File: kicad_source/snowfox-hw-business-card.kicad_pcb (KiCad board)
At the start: 2 copper layers, 85 x 54 mm, 109 parts, among them CN1 Micro_SDCard, CN2 CONN_02X05, CN3 CONN_01X24, CN4 USB_OTG, CN5 CONN_01X14, CN6 CONN_01X04, Q1 SI1304BDL, Q2 BC847, SW1 TAST_VER, SW2 TAST_VER, SW3 TAST_VER, SW4 TAST_VER, SW5 SWITCH_INV, U1 W25Q80D, U2 ATECC608A, U3 FE310-G002, U4 FT230XS, U5 TPS736XX, U6 TPS736XX, U7 M24LR, U8 BMA400, Y1 16MHz

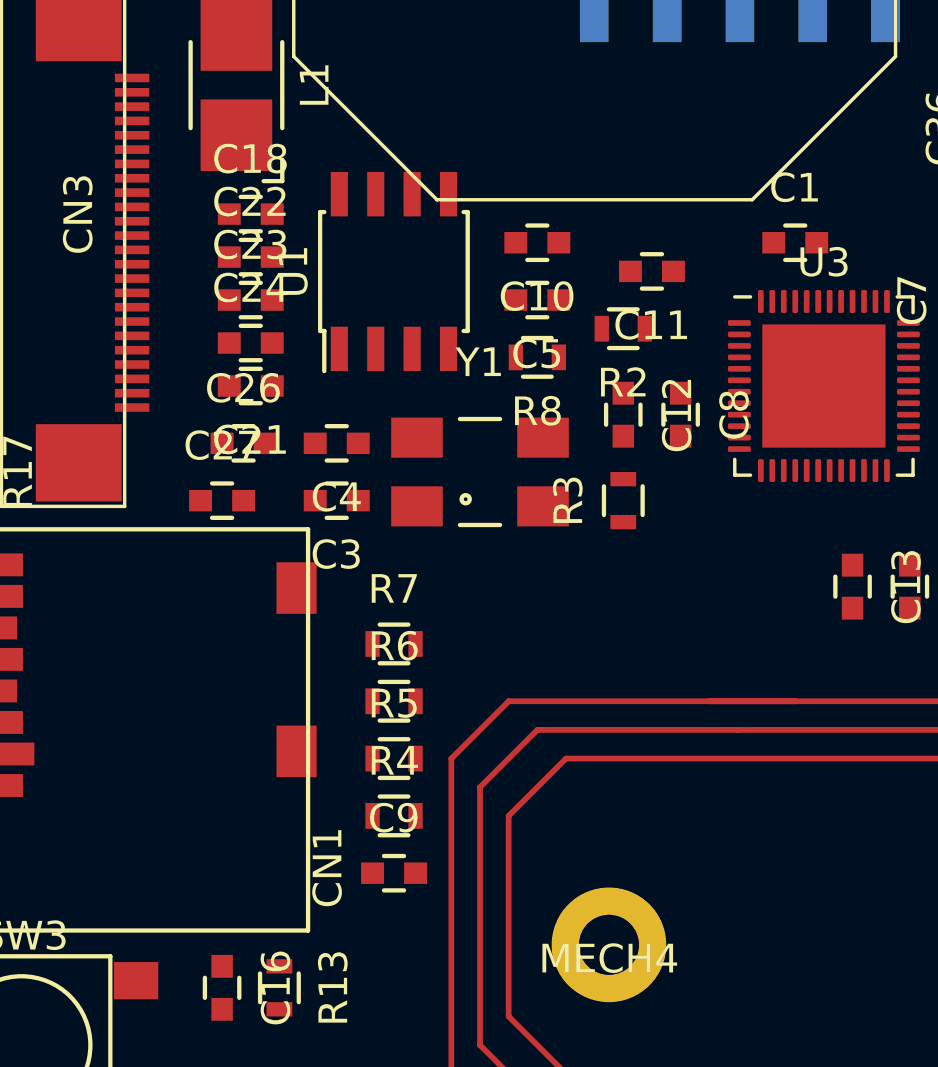
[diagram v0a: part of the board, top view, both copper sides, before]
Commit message: changed to smaller crystal footprint
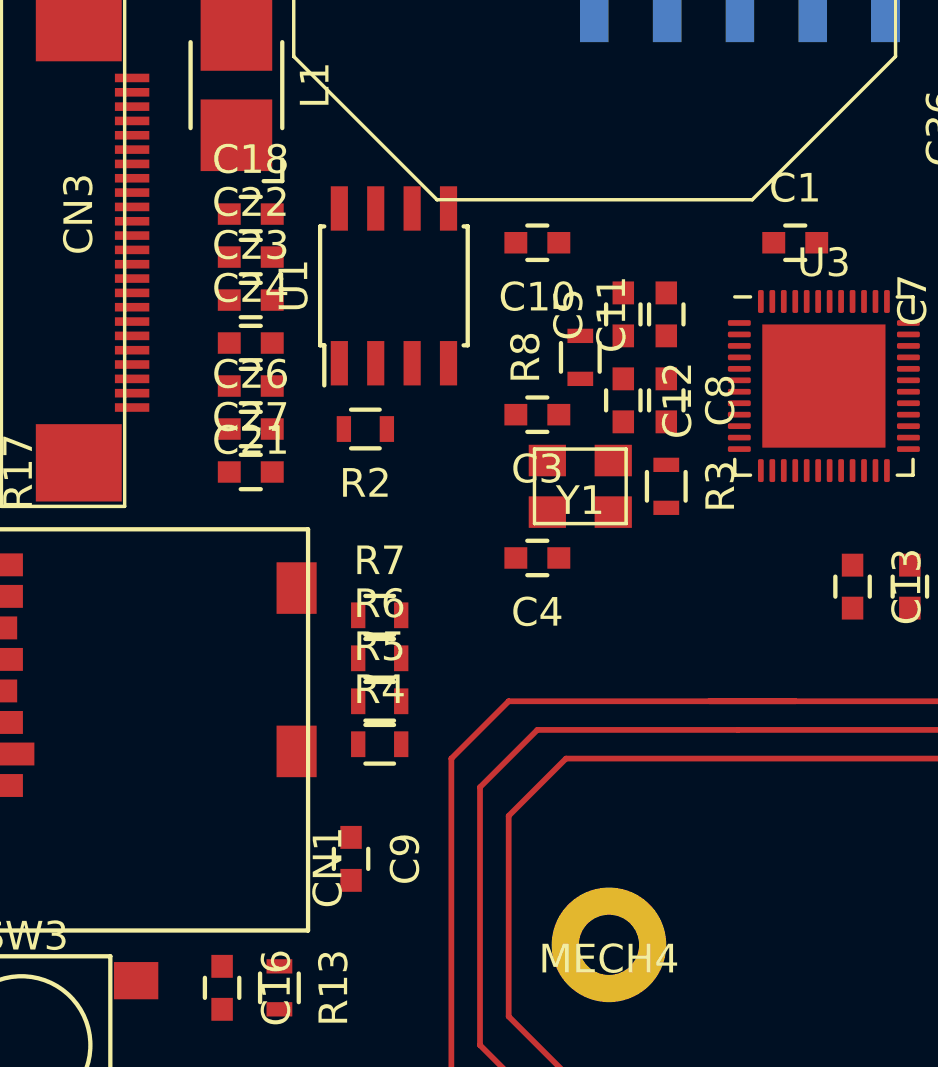
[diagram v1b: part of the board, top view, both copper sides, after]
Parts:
- Y1: footprint crystals:Crystal_SMD_0603_4Pads -> crystals:Crystal_SMD_3.2x2.5mm_4Pad
- moved R2 9.66 mm to (96.0, 111.5)
- moved C4 8.06 mm to (102.0, 116.0)
- moved C3 7.62 mm to (102.0, 111.0)
- moved Y1 3.54 mm to (103.5, 113.5)
- moved C5 3.04 mm to (105.0, 107.5), turned to 90 degrees
- moved R4 2.55 mm to (96.5, 122.5)
- moved R5 2.06 mm to (96.5, 121.0)
- moved C11 1.58 mm to (106.5, 107.5), turned to 90 degrees
- moved C9 1.58 mm to (95.5, 126.5), turned to 270 degrees
- moved R3 1.58 mm to (106.5, 113.5), turned to 270 degrees
- moved R6 1.58 mm to (96.5, 119.5)
- moved R8 1.50 mm to (103.5, 109.0), turned to 90 degrees
- moved C27 1.41 mm to (92.0, 113.0)
- moved R7 1.12 mm to (96.5, 118.0)
- moved C8 0.71 mm to (106.5, 110.5)
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
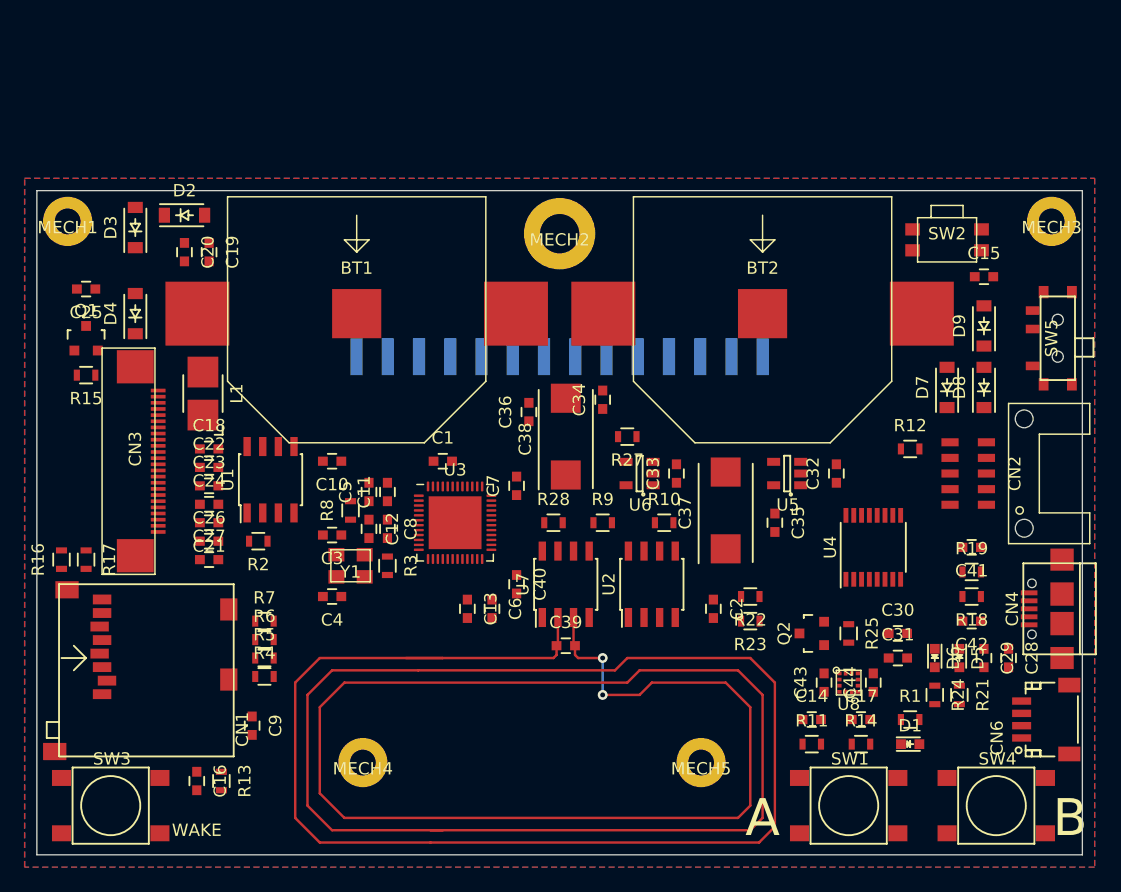
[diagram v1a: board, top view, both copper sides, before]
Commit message: routed some traces
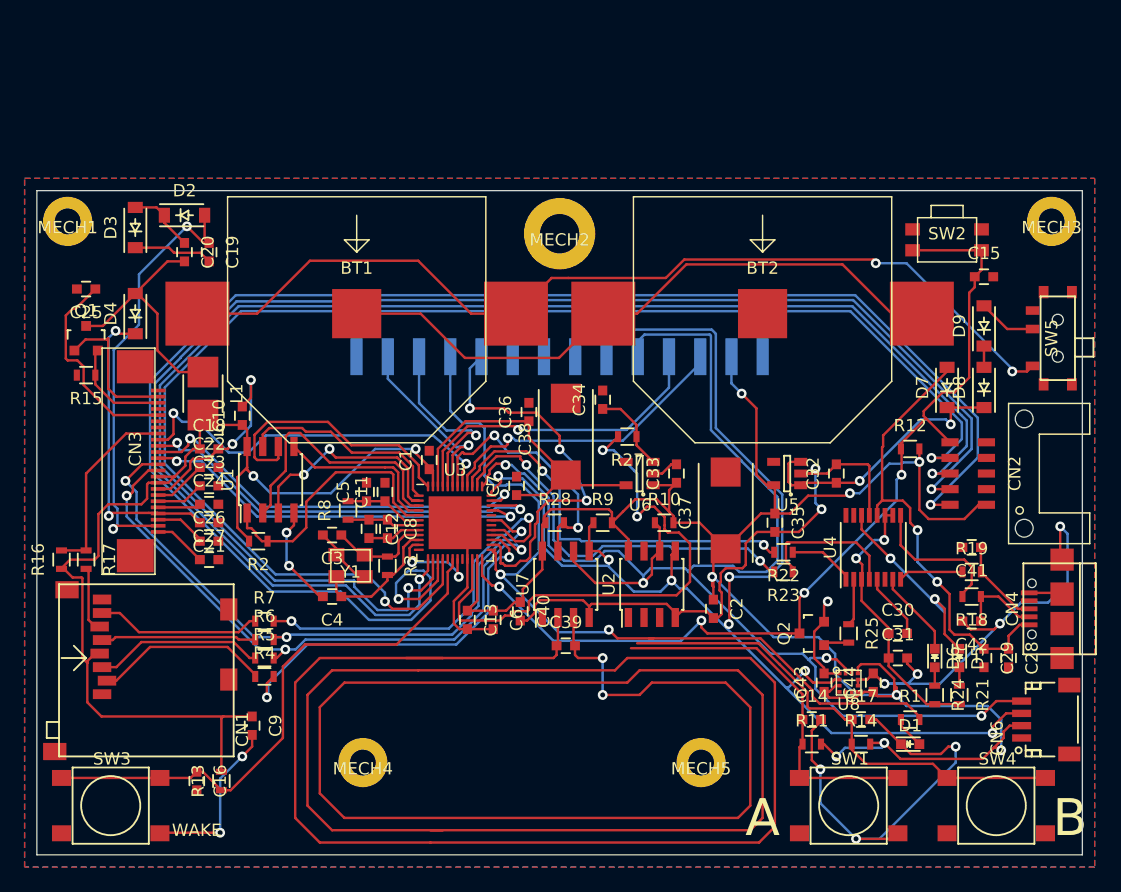
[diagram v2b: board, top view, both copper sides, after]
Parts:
- moved C10 8.18 mm to (94.7, 101.3), turned to 90 degrees
- moved R23 4.83 mm to (138.7, 114.0)
- moved R22 4.50 mm to (138.7, 112.4)
- moved C40 2.22 mm to (117.3, 117.2)
- moved C1 1.10 mm to (109.9, 104.9), turned to 90 degrees
- moved C6 0.91 mm to (115.1, 117.9)
- moved C13 0.90 mm to (113.0, 117.9)
- moved C11 0.20 mm to (106.3, 107.5)
- moved C5 0.20 mm to (104.8, 107.5)
- moved R8 0.20 mm to (103.3, 109.0)
- moved R28 0.10 mm to (120.1, 110.0)
- turned R13 to 90 degrees
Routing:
- net +3V3: track 0.00 -> 256.8 mm, vias 0 -> 12
- net GND: track 0.00 -> 208.4 mm, vias 0 -> 16
- net /Microcontroller/JTAG_TMS: track 0.00 -> 132.6 mm, vias 0 -> 2
- net /Microcontroller/JTAG_TCK: track 0.00 -> 119.5 mm, vias 0 -> 2
- net /Microcontroller/JTAG_TDO: track 0.00 -> 117.1 mm, vias 0 -> 2
- net /Microcontroller/JTAG_TDI: track 0.00 -> 114.0 mm, vias 0 -> 2
- net I2C_SCL: track 0.00 -> 112.4 mm, vias 0 -> 4
- net I2C_SDA: track 0.00 -> 110.5 mm, vias 0 -> 7
- net Net-(BT1-Pad1): track 0.00 -> 77.4 mm, vias 0 -> 2
- net RESET: track 0.00 -> 77.2 mm, vias 0 -> 4
- net /Microcontroller/LED: track 0.00 -> 67.2 mm, vias 0 -> 2
- net /Microcontroller/BUTTON_B: track 0.00 -> 55.1 mm, vias 0 -> 1
- net Net-(BT1-Pad2): track 0.00 -> 52.2 mm
- net SPI_MOSI: track 0.00 -> 51.9 mm, vias 0 -> 3
- net SPI_CLK: track 0.00 -> 51.6 mm, vias 0 -> 3
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
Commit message: changed diodes to smaller footprint, connected all lines in layout, updated images
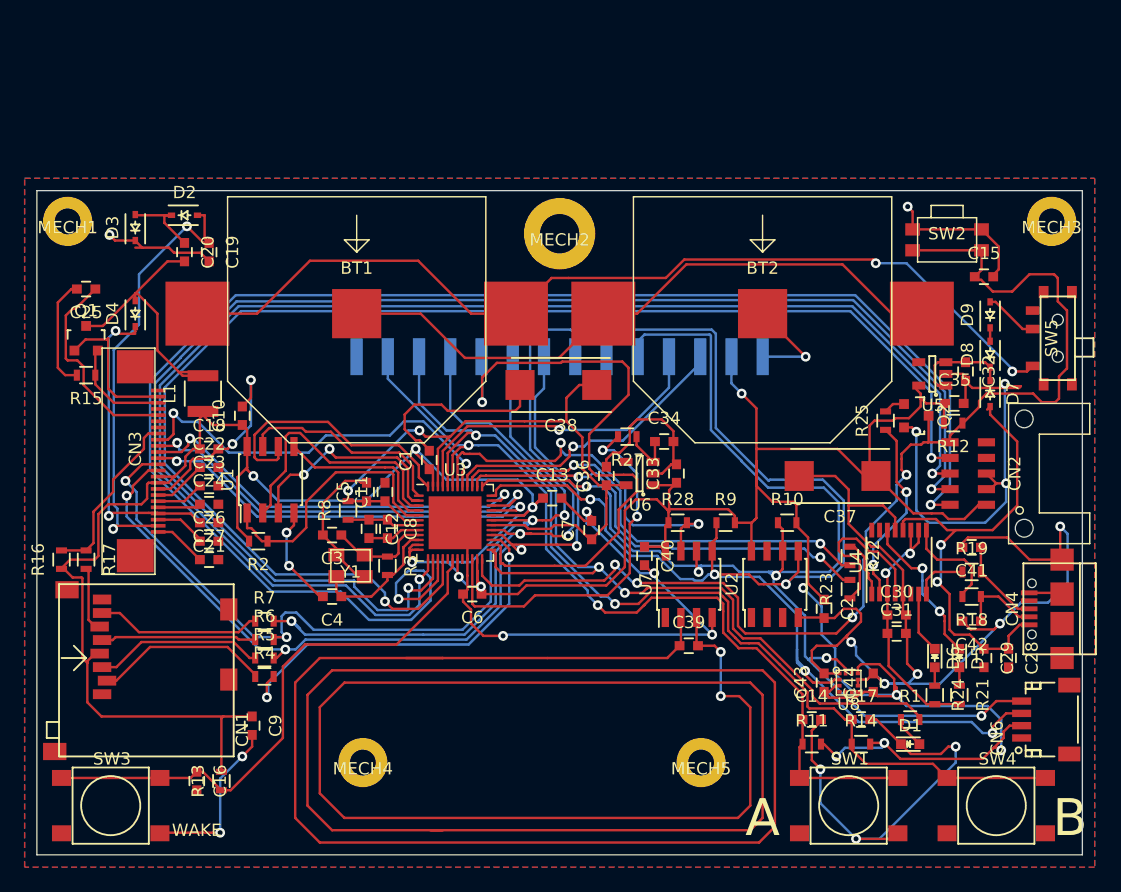
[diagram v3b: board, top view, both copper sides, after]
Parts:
- D2, D3, D4, D7: value MBR0530 -> B0530WS; footprint diodes:SOD-123 -> diodes:SOD-323
- D8, D9: value 1N4148 -> 1N4148WS; footprint diodes:SOD-123 -> diodes:SOD-323
- L1: footprint inductors:Inductor_1212 -> resistors:R_1210
- moved Q2 19.6 mm to (149.5, 101.3), turned to 270 degrees
- moved R25 17.6 mm to (147.0, 101.7), turned to 90 degrees
- moved C35 17.5 mm to (152.6, 100.3), turned to 0 degrees
- moved U5 14.3 mm to (150.8, 97.9)
- moved C32 13.4 mm to (153.5, 97.7), turned to 270 degrees
- moved C13 12.1 mm to (119.9, 108.0), turned to 0 degrees
- moved C40 11.1 mm to (127.4, 112.7)
- moved C39 10.0 mm to (131.0, 120.0)
- moved R10 10.0 mm to (139.0, 110.0)
- moved R28 10.0 mm to (130.1, 110.0)
- moved R9 10.0 mm to (134.0, 110.0)
- moved U2 10.0 mm to (138.0, 115.0)
- moved U7 10.0 mm to (131.0, 115.0)
- moved C37 9.52 mm to (143.1, 106.2), turned to 180 degrees
- moved C2 9.00 mm to (142.0, 117.0)
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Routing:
- net GND: track 208.4 -> 344.5 mm, vias 16 -> 24
- net +3V3: track 256.8 -> 300.0 mm
- net SPI_MISO: track 31.9 -> 58.3 mm, vias 2 -> 3
- net +1V8: track 33.2 -> 59.2 mm, vias 0 -> 2
- net /Microcontroller/BUTTON_A: track 45.3 -> 70.6 mm, vias 1 -> 2
- net /Microcontroller/BUTTON_B: track 55.1 -> 80.0 mm, vias 1 -> 2
- net SPI_CLK: track 51.6 -> 75.5 mm, vias 3 -> 4
- net SPI_MOSI: track 51.9 -> 74.8 mm, vias 3 -> 4
- net RESET: track 77.2 -> 96.7 mm
- net /Microcontroller/GPIO_1: track 32.0 -> 50.1 mm, vias 3 -> 1
- net VCC: track 22.7 -> 8.26 mm, vias 2 -> 0
- net VDD_CORE_EN: track 44.3 -> 31.3 mm
- net /USB/RTS: track 3.82 -> 15.8 mm, vias 0 -> 2
- net NFC_BUSY: track 21.6 -> 31.6 mm
- net I2C_SDA: track 110.5 -> 117.4 mm, vias 7 -> 5
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
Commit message: made pcb edges round, added slot for mounting
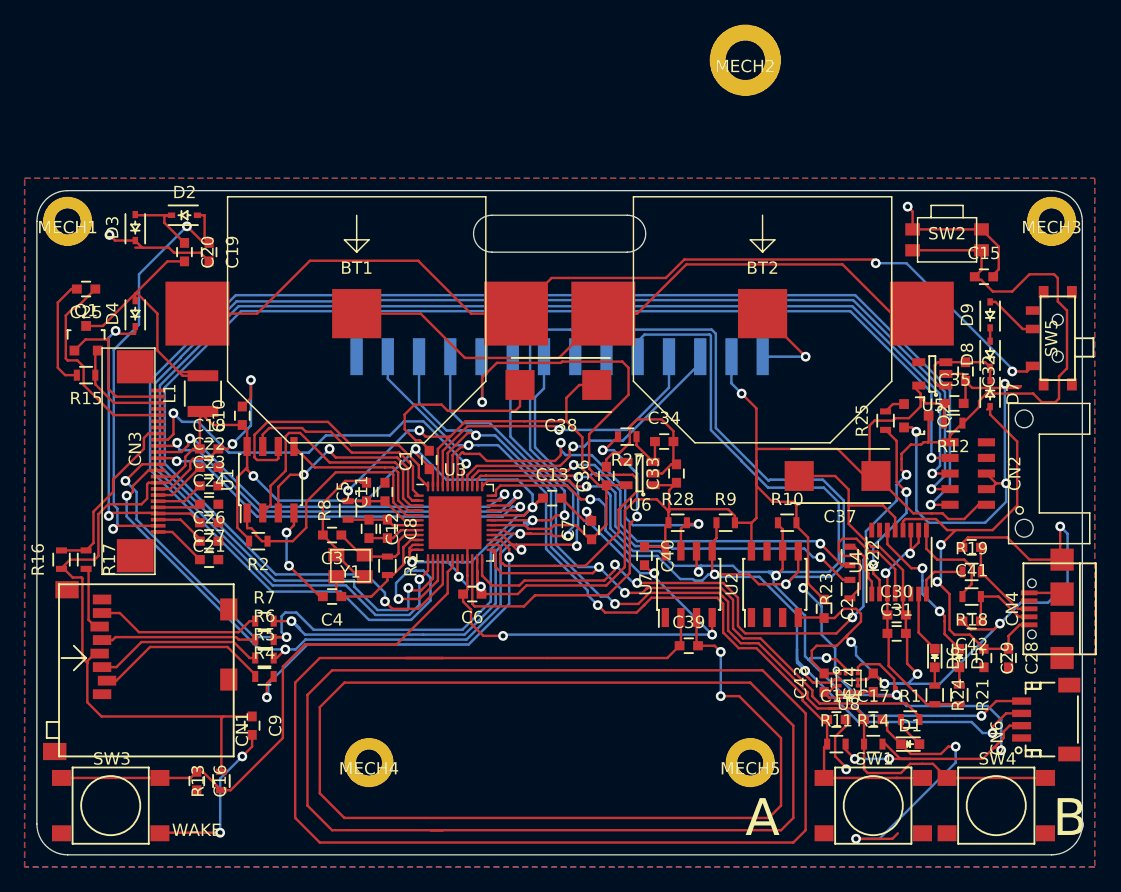
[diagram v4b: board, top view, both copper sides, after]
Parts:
- moved MECH2 20.7 mm to (135.6, 72.4)
- moved MECH5 4.00 mm to (136.0, 129.5)
- moved C14 2.00 mm to (143.0, 126.0)
- moved R11 2.00 mm to (143.0, 128.0)
- moved SW1 2.00 mm to (146.0, 133.0)
- moved C17 1.00 mm to (146.0, 126.0)
- moved R14 1.00 mm to (146.0, 128.0)
- moved MECH4 0.50 mm to (105.0, 129.5)
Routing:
- net /NFC/ANTENNA: track 297.7 -> 308.4 mm
- net GND: track 344.5 -> 337.1 mm
- net /Microcontroller/BUTTON_B: track 80.0 -> 81.9 mm
- net +3V3: track 300.0 -> 298.6 mm
- net /Microcontroller/BUTTON_A: track 70.6 -> 71.9 mm
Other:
- outline, holes or cut-outs redrawn

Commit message: rearranged parts for display
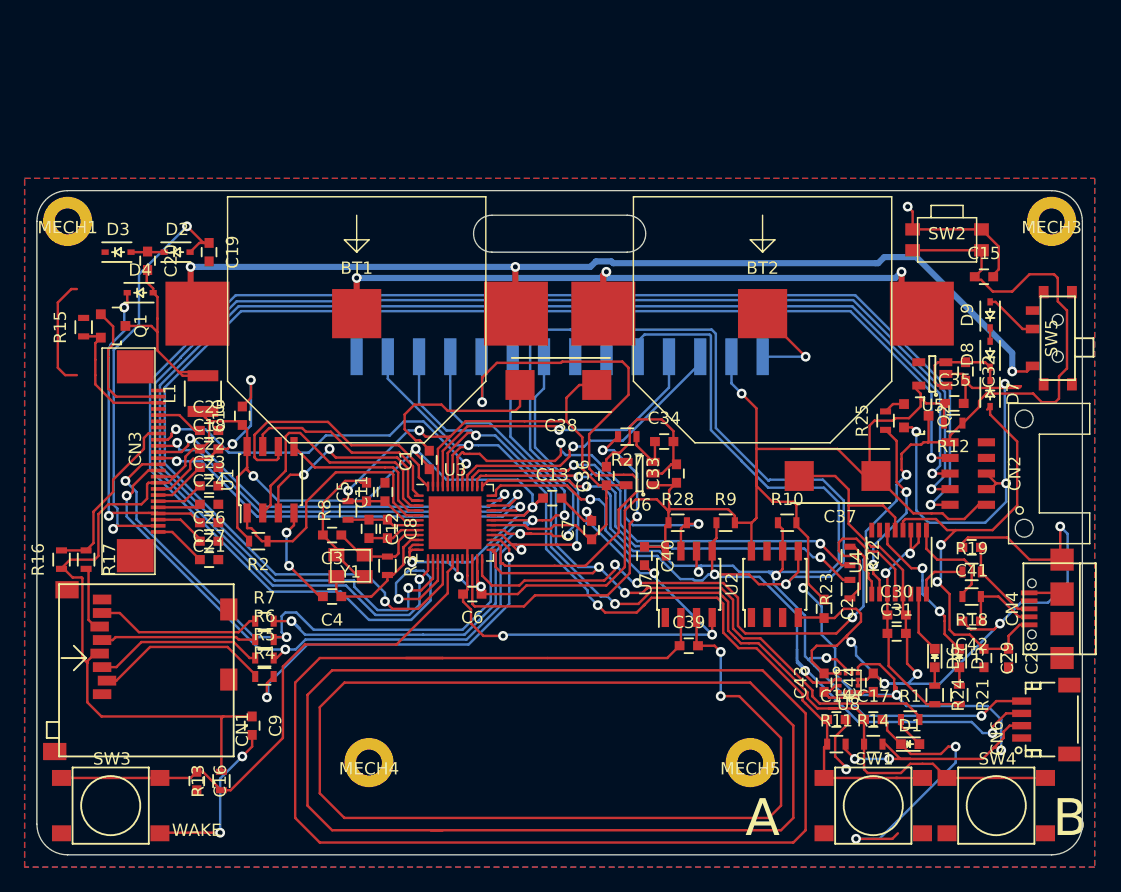
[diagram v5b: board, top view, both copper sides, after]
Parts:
- removed MECH2: MHP_3.2_5.8, MECH_mounting_holes:MHP_3.2_5.8
- moved C25 15.2 mm to (92.0, 102.5), turned to 0 degrees
- moved R15 3.91 mm to (81.8, 94.1), turned to 90 degrees
- moved C20 3.08 mm to (87.0, 88.7)
- moved D2 3.06 mm to (89.4, 88.0)
- moved D3 2.44 mm to (84.6, 88.0), turned to 0 degrees
- moved Q1 2.42 mm to (84.2, 94.0), turned to 270 degrees
- moved D4 1.75 mm to (86.4, 91.3), turned to 0 degrees
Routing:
- net /Display/VSH2: track 17.1 -> 3.91 mm
- net GND: track 337.1 -> 327.5 mm, vias 24 -> 23
- net Net-(C20-Pad2): track 22.7 -> 16.2 mm
- net Net-(BT1-Pad1): track 77.4 -> 81.7 mm, vias 2 -> 3
- net Net-(C20-Pad1): track 6.48 -> 2.73 mm
- net Net-(BT1-Pad2): track 52.2 -> 55.6 mm, vias 0 -> 3
- net /Display/RESE: track 8.56 -> 11.2 mm
- net DIS_BUSY: track 32.6 -> 30.7 mm
- net /Display/VGH: track 25.5 -> 26.6 mm
- net /Display/VGL: track 36.4 -> 35.3 mm
- net /Display/GDR: track 11.6 -> 11.0 mm

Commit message: reworked silk screen
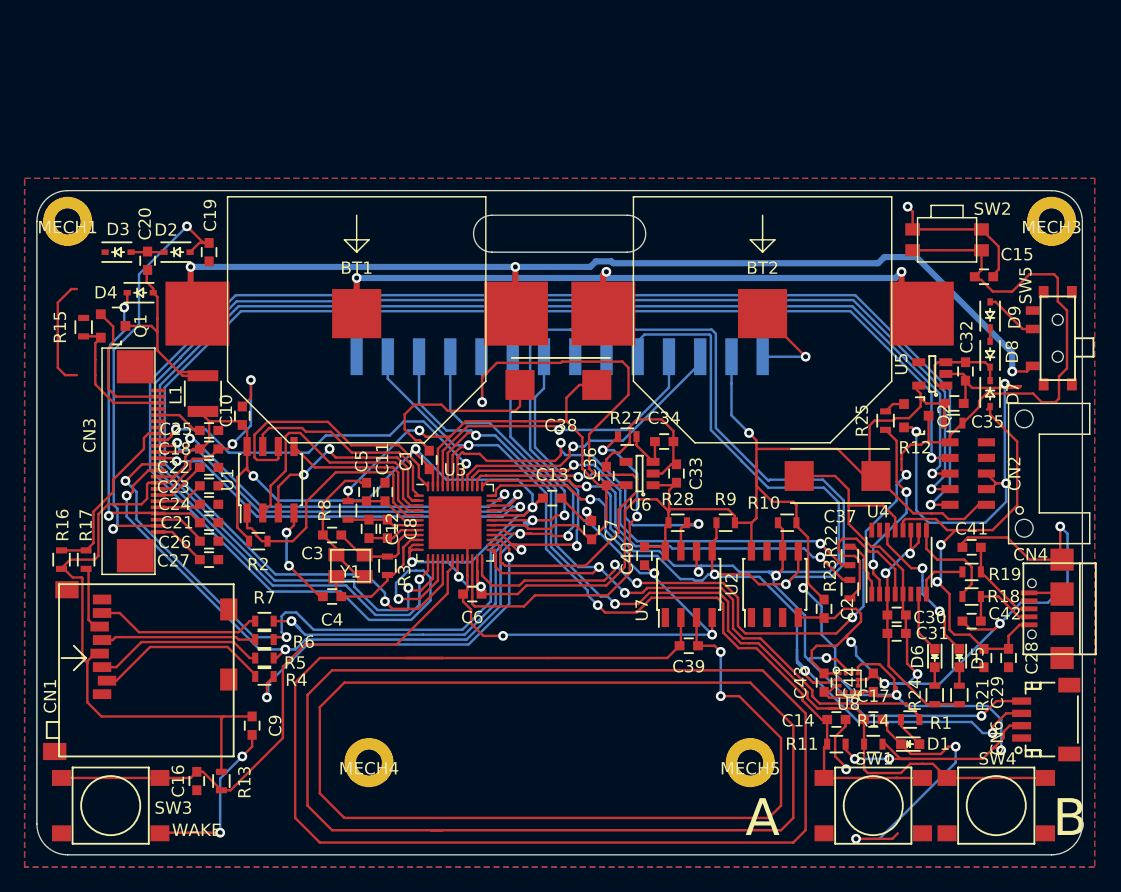
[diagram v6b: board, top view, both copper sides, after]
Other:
- board text added: "+3V3"
- board text added: "BUTTON A"
- board text added: "BUTTON B"
- board text added: "CLK"
- board text added: "GND"
- board text added: "GPIO 1"
- board text added: "LED"
- board text added: "MISO"
- board text added: "MOSI"
- board text added: "RX"
- board text added: "SCL"
- board text added: "SDA"
- board text added: "TX"
